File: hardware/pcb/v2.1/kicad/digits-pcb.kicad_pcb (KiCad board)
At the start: 2 copper layers, 61.9 x 76.2 mm, 77 parts, among them J1 Conn_02x20_Odd_Even, J3 VIN_BARREL_PIGTAIL, J4 Conn_01x07, J6 Conn_01x02, J7 Screw_Terminal_01x02, J8 Conn_01x04, SW1 Hook_DPDT, SW2 SW_Push, U10 XL6019E1, U2 DRV8871DDAR, U3 RP2040, U4 W25Q16JVSSIQ, U5 AMS1117-3.3, U6 TLV320AIC3104IRHBR, U7 XC6206P182MR, Y1 ABM8-272-T3

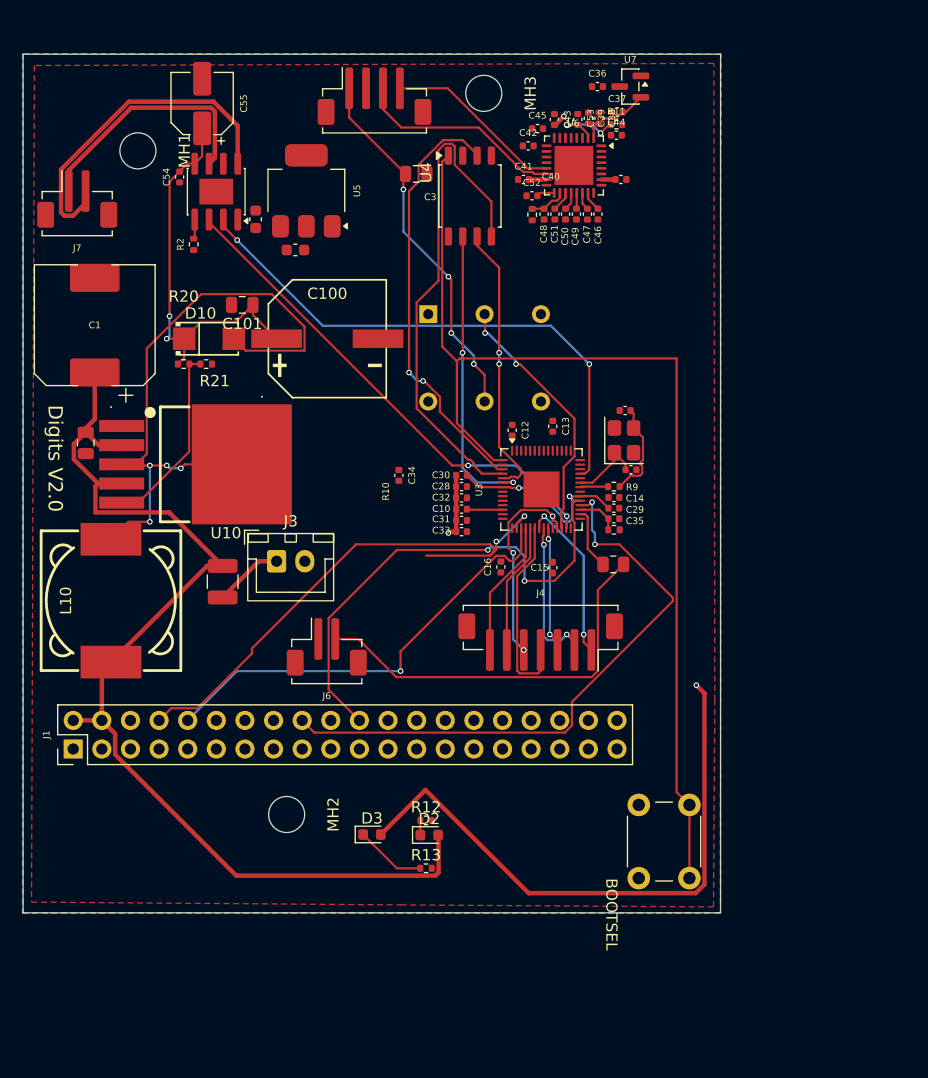
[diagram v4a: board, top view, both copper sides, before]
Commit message: wip(hardware): auto-route pass + solid-zone fix eliminates all zone islands
Partial routing progress on V2.1, banked before attempting a full re-route.
Not fab-ready; intermediate checkpoint.

- Freerouting got the board to ~838 traces / 99 vias (most nets routed).
- Zone islands: 11 orphaned GND fragments (at the J1 pad row) -> 0. Fix was
  switching both pours (GND on B.Cu, +3V3 on F.Cu) from thermal-relief to
  solid pad connection: the J1 GND pads and QFN power pads sat inside the pour
  but were thermally starved (a 0.2mm pad cannot form a 0.3mm thermal spoke),
  so solid bonding tied them in and cleared all 11 islands plus 5
  starved-thermal errors at once. Sound for power/ground planes on reflow.
- MIC_FROM_SW routed end to end (R10.1<->C46.1<->SW1.4).

Verified DRC: 0 shorts, 0 clearance, 0 thermal, 0 islands. Remaining: 12 DFM
errors (7 hole-clearance, 5 board-edge-clearance from freerouting vias) and 20
unconnected ratsnest lines (CODEC_BCLK, CODEC_DOUT, UART_TX_PI, QSPI_SD1,
DVDD_1V1 plus the power-pour endpoints). These trace to J1 sitting in a
congested channel; J1 orientation is fixed by the enclosure and will not
change, so the remaining nets get a full global re-route attempt next.

netclass config is unchanged from the committed V2 reference (0.13mm).
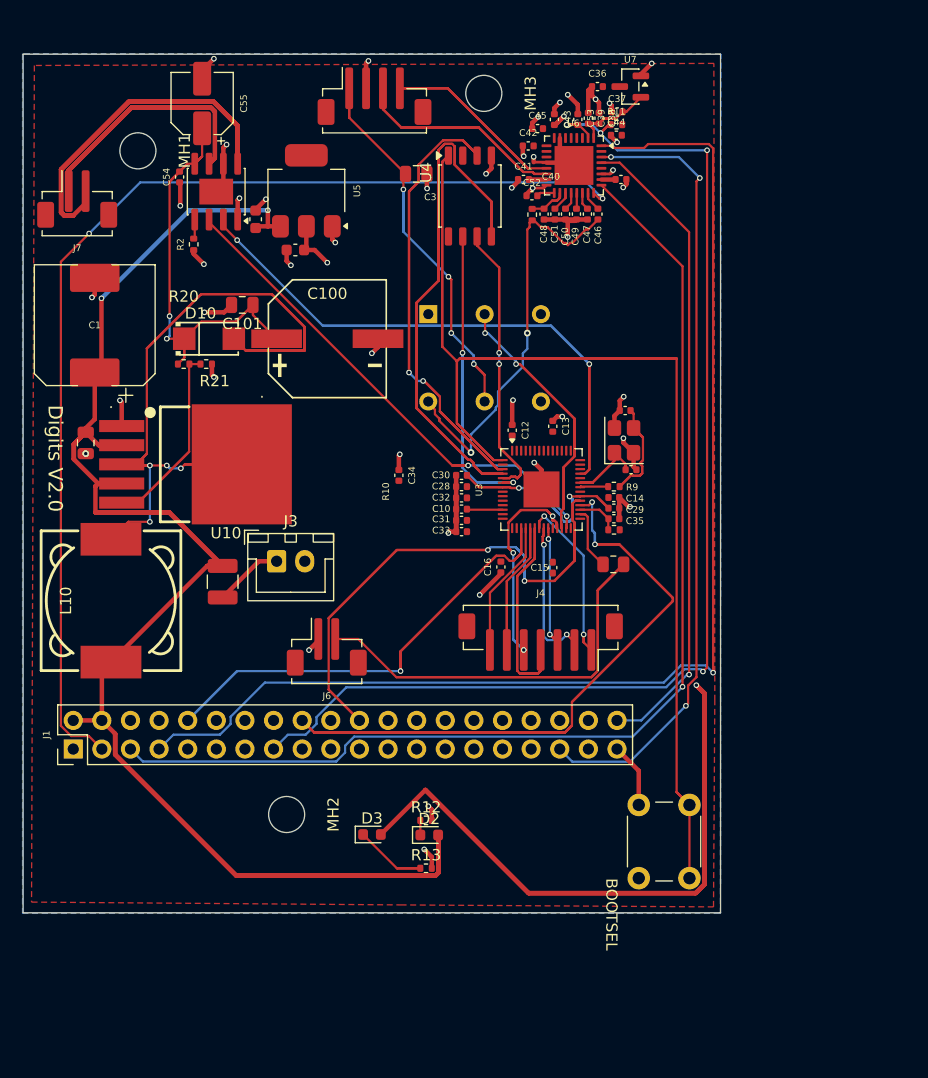
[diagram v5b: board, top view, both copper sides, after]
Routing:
- net CODEC_MCLK: track 0.00 -> 109.7 mm, vias 0 -> 1
- net CODEC_RESET: track 7.11 -> 110.5 mm, vias 2 -> 4
- net CODEC_SCL: track 0.00 -> 100.1 mm, vias 0 -> 1
- net CODEC_SDA: track 0.00 -> 98.3 mm, vias 0 -> 2
- net GND: track 5.73 -> 102.6 mm, vias 1 -> 43
- net +5V: track 94.8 -> 183.2 mm, vias 0 -> 2
- net CODEC_WCLK: track 0.00 -> 70.6 mm, vias 0 -> 3
- net CODEC_DIN: track 0.00 -> 57.7 mm, vias 0 -> 1
- net +3V3: track 56.4 -> 109.1 mm, vias 2 -> 3
- net BELL_B: track 30.1 -> 82.1 mm
- net UART_TX_PI: track 49.4 -> 0.00 mm, vias 2 -> 0
- net QSPI_SS: track 96.1 -> 144.7 mm
- net SWD_SWDIO: track 53.6 -> 101.8 mm
- net QSPI_SD0: track 45.0 -> 89.7 mm
- net LED_A: track 35.3 -> 74.2 mm
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
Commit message: wip(hardware): full global re-route - 0 DRC errors, 4 nets + 3V3 slivers left
Ripped up all tracks and re-routed the board from scratch with headless
freerouting (--gui.enabled=false, the flag that makes it write the SES and
exit instead of hanging). The global route threaded the J1-channel congestion
the stuck incremental route could not.

Result vs the 8e8c4db2 baseline (12 errors / 20 unconnected): now 0 hard
errors / 13 unconnected. Strictly better on both axes.

Key technique: pcbnew exports the netclass clearance (0.13mm) into the DSN, but
KiCad enforces a separate 0.25mm hole-clearance rule freerouting does not model,
so a native-clearance import lands tracks ~0.23mm from via barrels and trips 51
hole-clearance errors. Bumping the DSN clearance to 0.155mm pushes tracks off
the barrels while still completing most nets (swept 0.145-0.17mm; 0.155 was the
sweet spot). The one remaining board-edge via was nudged 0.25mm inward.

Verified: 0 shorts, 0 clearance, 0 tracks-crossing, 0 thermal, 0 mask-bridge.
J1 untouched (17.199, 73.876, 90deg - enclosure-fixed). Zones still solid
pad-connection. .kicad_pro and schematic unchanged.

Remaining 13 unconnected: 9 are floating +3V3 copper slivers (the F.Cu pour
fragmented; no B.Cu +3V3 pour to via-stitch to - clear via remove-islands or
leave as dead copper, no functional impact). 4 are real nets stuck in the
densest codec/RP2040 regions: GND->U3.19, +1V8 C38<->C37, CODEC_DIN U6<->J1,
QSPI_SCLK U4<->U3. Every manual attempt at those reintroduced shorts/crossings,
so they're left for careful interactive routing rather than trading away 0
errors.
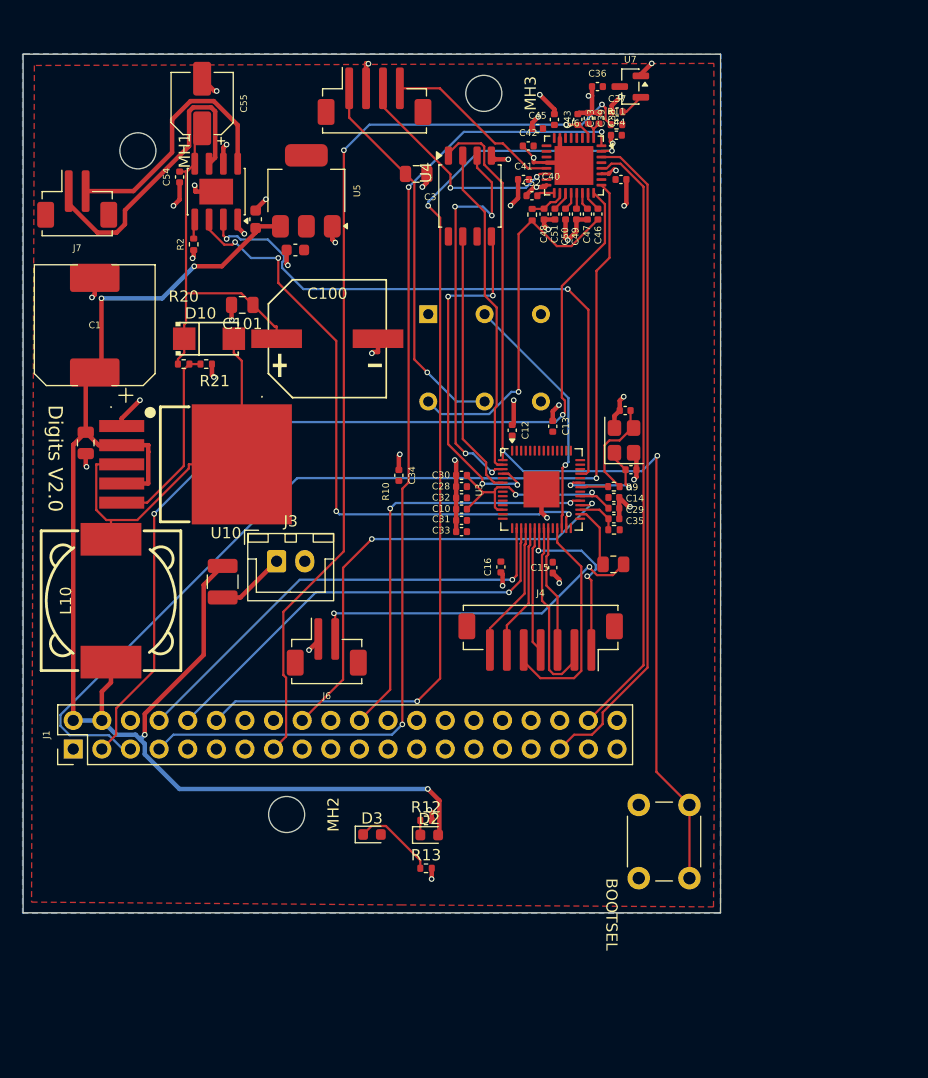
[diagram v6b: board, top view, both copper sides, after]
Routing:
- net +3V3: track 109.1 -> 0.00 mm, vias 3 -> 0
- net CODEC_BCLK: track 0.00 -> 83.3 mm, vias 0 -> 3
- net /ringer/SW_NODE: track 96.7 -> 35.0 mm, vias 4 -> 0
- net SWD_SWDIO: track 101.8 -> 40.6 mm
- net BELL_B: track 82.1 -> 22.8 mm
- net QSPI_SS: track 144.7 -> 86.2 mm, vias 0 -> 2
- net CODEC_DIN: track 57.7 -> 0.00 mm, vias 1 -> 0
- net QSPI_SD0: track 89.7 -> 32.2 mm, vias 0 -> 4
- net CODEC_DOUT: track 0.00 -> 54.1 mm
- net +5V: track 183.2 -> 132.1 mm, vias 2 -> 4
- net QSPI_SCLK: track 45.2 -> 0.00 mm, vias 2 -> 0
- net LED_A: track 74.2 -> 30.5 mm, vias 0 -> 2
- net SWD_SWCLK: track 78.8 -> 37.1 mm
- net UART_TX_PI: track 0.00 -> 41.3 mm, vias 0 -> 1
- net QSPI_SD2: track 70.4 -> 35.9 mm, vias 2 -> 4
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
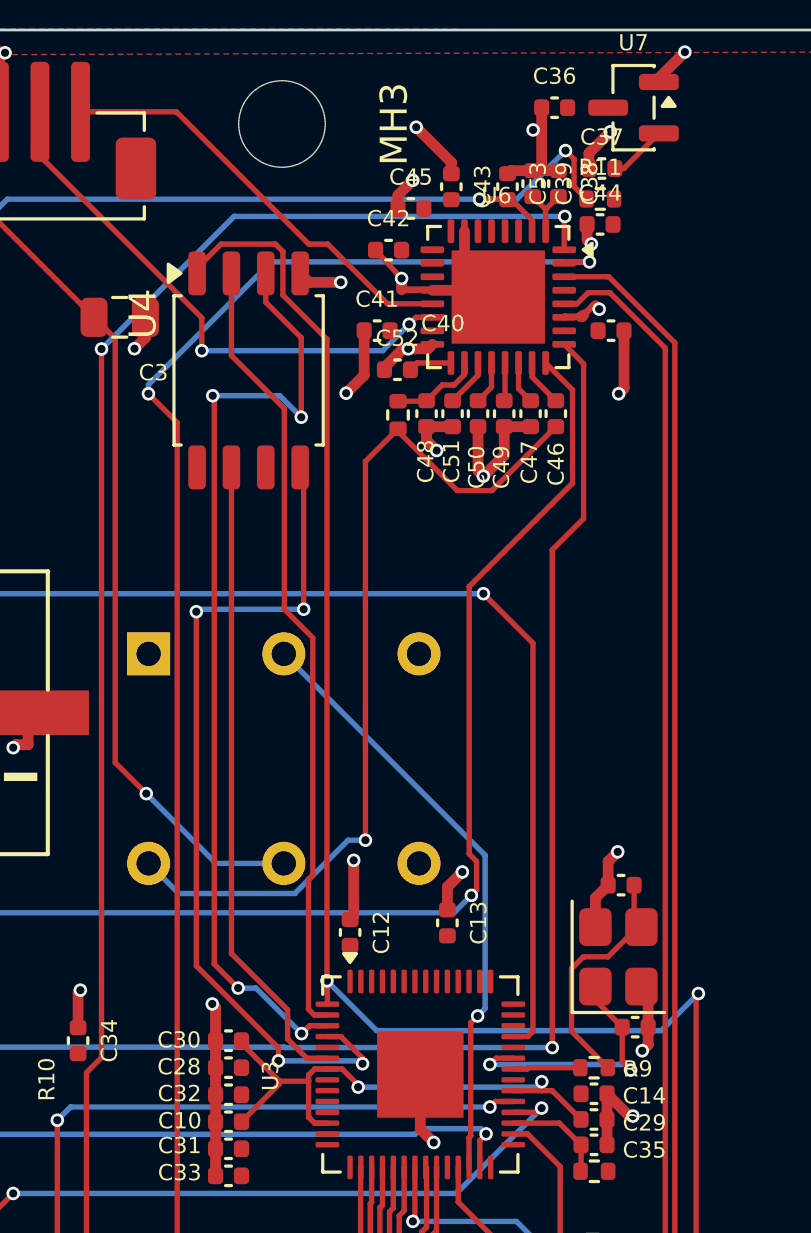
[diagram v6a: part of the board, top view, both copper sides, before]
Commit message: wip(hardware): route QSPI_SCLK and +1V8 - down to 2 real unconnected nets
Surgical follow-up to the global re-route. Routed 2 of the 4 stuck nets while
holding 0 DRC errors; unconnected 13 -> 11.

- /codec/+1V8 (C38.1<->C37.1): F.Cu stub, via to B.Cu, run east under the
  GND/CODEC_RESET wall, via back up at C37.1. 2 vias.
- QSPI_SCLK (U4.6<->U3.52): required a 3-net re-fan. SCLK had no copper and
  U3.52's west escape was blocked by the QSPI_SD3 diagonal, which was itself
  boxed by QSPI_SD0. Ripped SD0/SD3/SCLK (all simple U4<->U3 2-pad nets) and
  re-fanned as parallel breakouts: SCLK 0 vias, SD3 0 vias, SD0 4 vias. All at
  the board's 0.2mm min_track_width (sub-0.2 necking is itself a DRC error, so
  no thinner segments were used).

Remaining 2 real nets (genuine 2-layer wall in the codec/RP2040 corner):
- GND -> U3.19: RP2040 GND in the saturated XIN/XOUT/SWD cluster; the only via
  band is blocked by the CODEC_SCL B.Cu track. Needs rerouting a J1 signal to
  open, disproportionate, left to protect 0-error state.
- CODEC_DIN U6.4 <-> J1.40: a true 3-way crossing in the codec I2S fan (codec
  pin order WCLK/DIN/DOUT vs J1 order WCLK/DOUT/DIN); only 2 of 3 escapes fit
  the funnel on 2 layers regardless of routing order.

The 9 +3V3 "unconnected" are pad-touching pour fragments not joined to the main
+3V3 region; with +3V3 only on F.Cu there is no clean 2-layer bridge.

Verified: 0 shorts/clearance/crossing/thermal/edge/hole. J1 untouched, zones
solid, .kicad_pro and schematic unchanged.
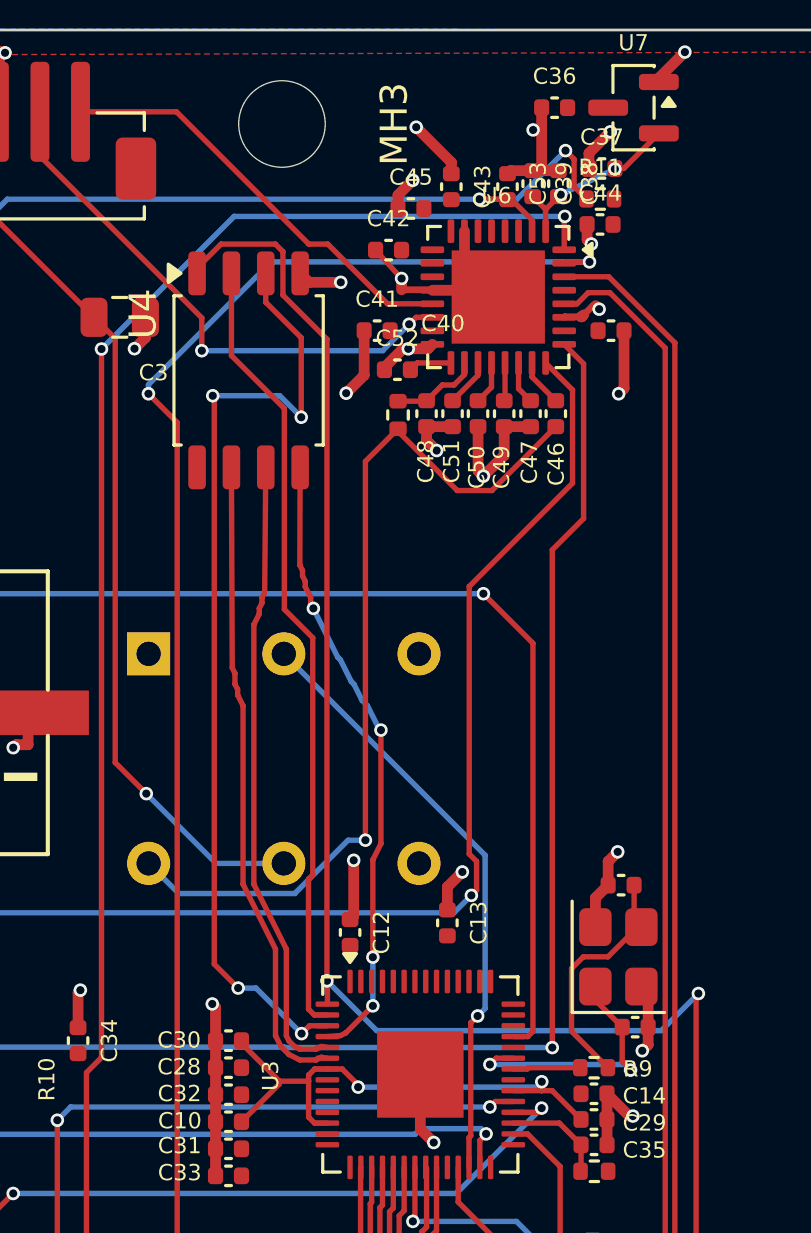
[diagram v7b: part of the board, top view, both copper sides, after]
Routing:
- net QSPI_SCLK: track 0.00 -> 23.2 mm
- net QSPI_SD0: track 32.2 -> 22.9 mm
- net /codec/+1V8: track 4.31 -> 6.65 mm, vias 0 -> 2

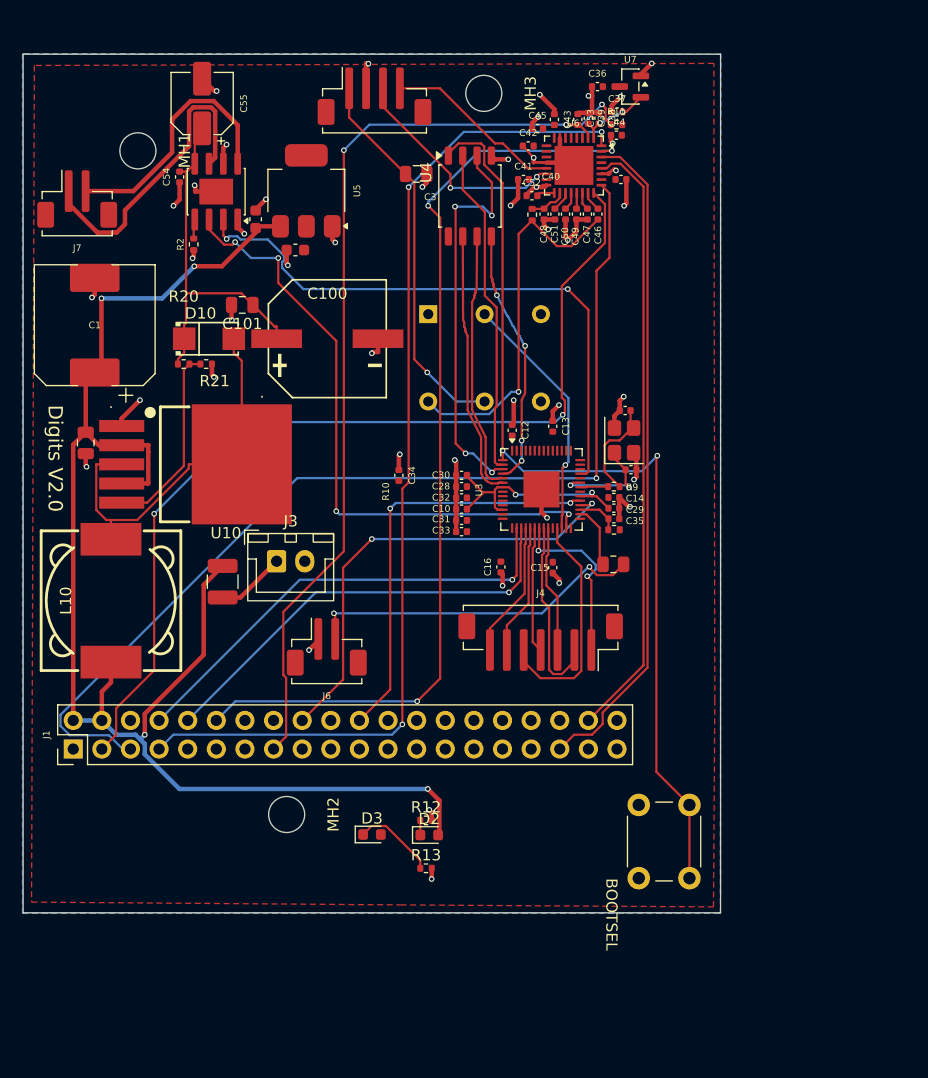
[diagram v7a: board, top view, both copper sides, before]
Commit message: feat(hardware): complete PCB routing - 0 DRC errors, 0 unconnected
Hand-routed the last 2 signal nets (CODEC_DIN U6.4<->J1.40, GND->U3.19) and
stitched the 9 orphaned +3V3 pour fragments to the main pour. Board is now
fully routed on 2 layers.

DRC: 0 errors, 0 unconnected. Remaining 68 warnings are pre-existing cosmetic
items (silkscreen clip/clearance, lib_footprint_mismatch) carried from V2,
none introduced by routing.

This closes the V2.1 routing effort: started at 78 unrouted nets, reached a
clean fully-routed 2-layer board with the on-board boost (37V), DPDT hook
switch, 5V input, and power LEDs all in place. J1 stayed enclosure-fixed
throughout; zones are solid pad-connection; schematic and netclasses unchanged.
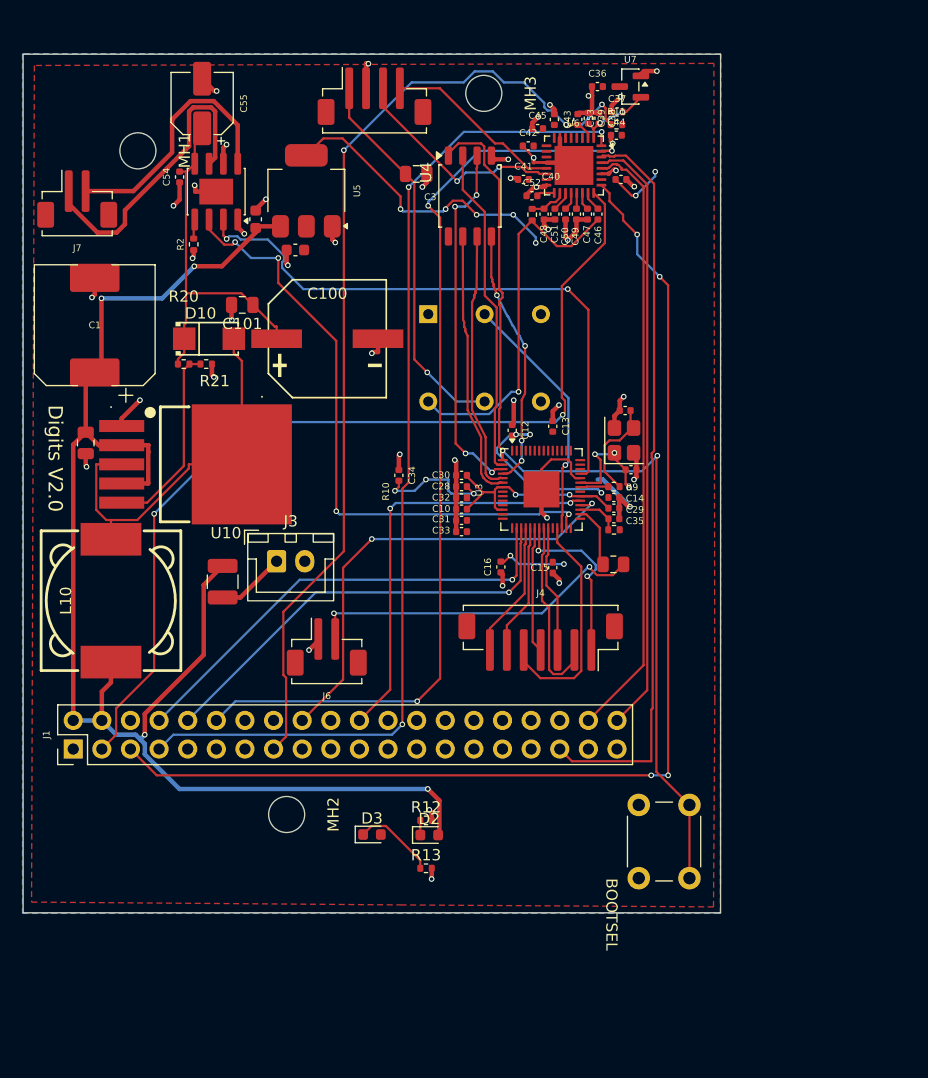
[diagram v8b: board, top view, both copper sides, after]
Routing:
- net +3V3: track 0.00 -> 64.7 mm, vias 0 -> 15
- net CODEC_DIN: track 0.00 -> 53.7 mm
- net CODEC_SCL: track 91.1 -> 103.5 mm, vias 1 -> 4
- net CODEC_WCLK: track 59.4 -> 65.8 mm
- net GND: track 95.3 -> 101.6 mm
- net CODEC_RESET: track 85.3 -> 89.5 mm
- net QSPI_SD2: track 35.9 -> 32.3 mm
- net EAR_P: track 20.4 -> 19.7 mm
- net XIN: track 9.88 -> 10.0 mm, vias 2 -> 3
